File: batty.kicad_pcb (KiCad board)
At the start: 2 copper layers, 137.4 x 95.2 mm, 102 parts, among them J1 MJ-4PP-9, J2 OLED, J3 LED, P1 i2c-pin, P2 i2c-pin, SW1 SW_PUSH, SW10 SW_PUSH, SW11 SW_PUSH, SW12 SW_PUSH, SW13 SW_PUSH, SW14 SW_PUSH, SW15 SW_PUSH, SW16 SW_PUSH, SW17 SW_PUSH, SW18 SW_PUSH, SW19 SW_PUSH, SW2 SW_PUSH, SW20 SW_PUSH, SW21 SW_PUSH, SW22 SW_PUSH, SW23 SW_PUSH, SW3 SW_PUSH, SW4 SW_PUSH, SW5 SW_PUSH, SW6 SW_PUSH, SW7 SW_PUSH, SW8 SW_PUSH, SW9 SW_PUSH, U1 ProMicro

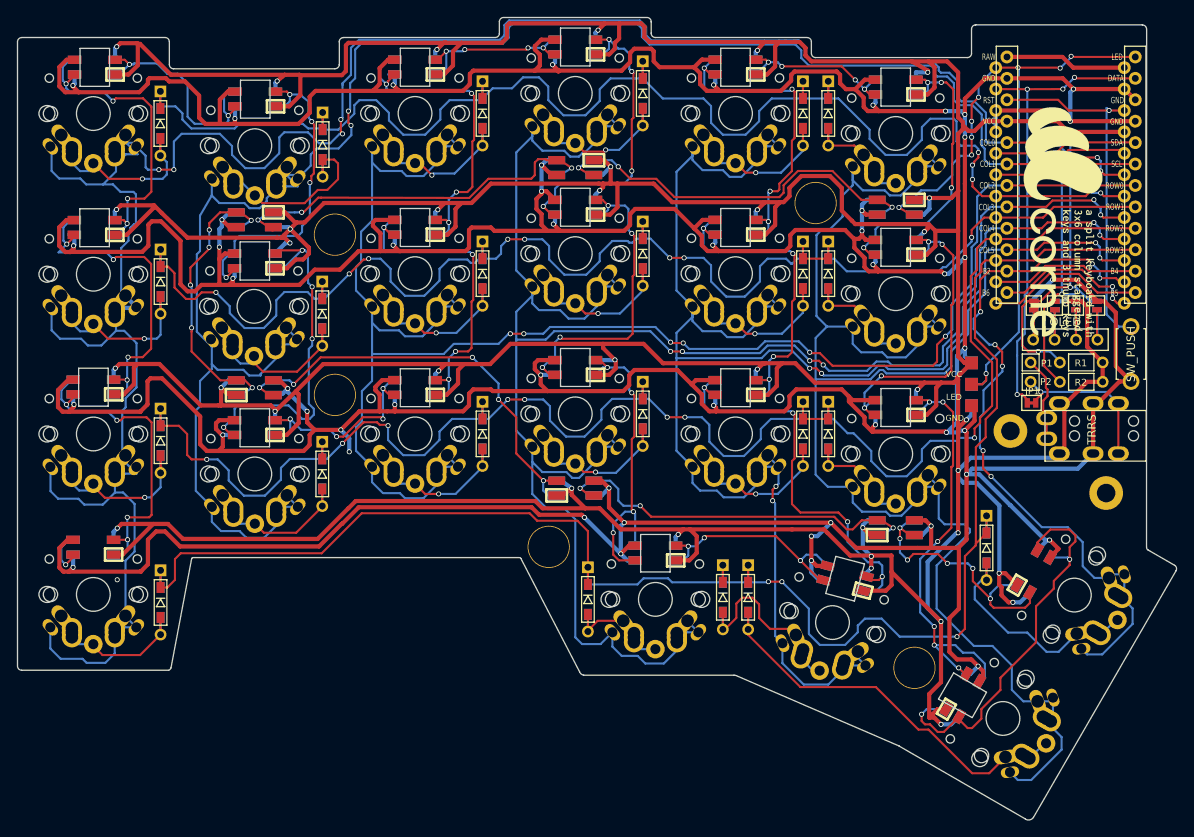
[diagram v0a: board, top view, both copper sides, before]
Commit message: add missing hole, update crkbd logo position.
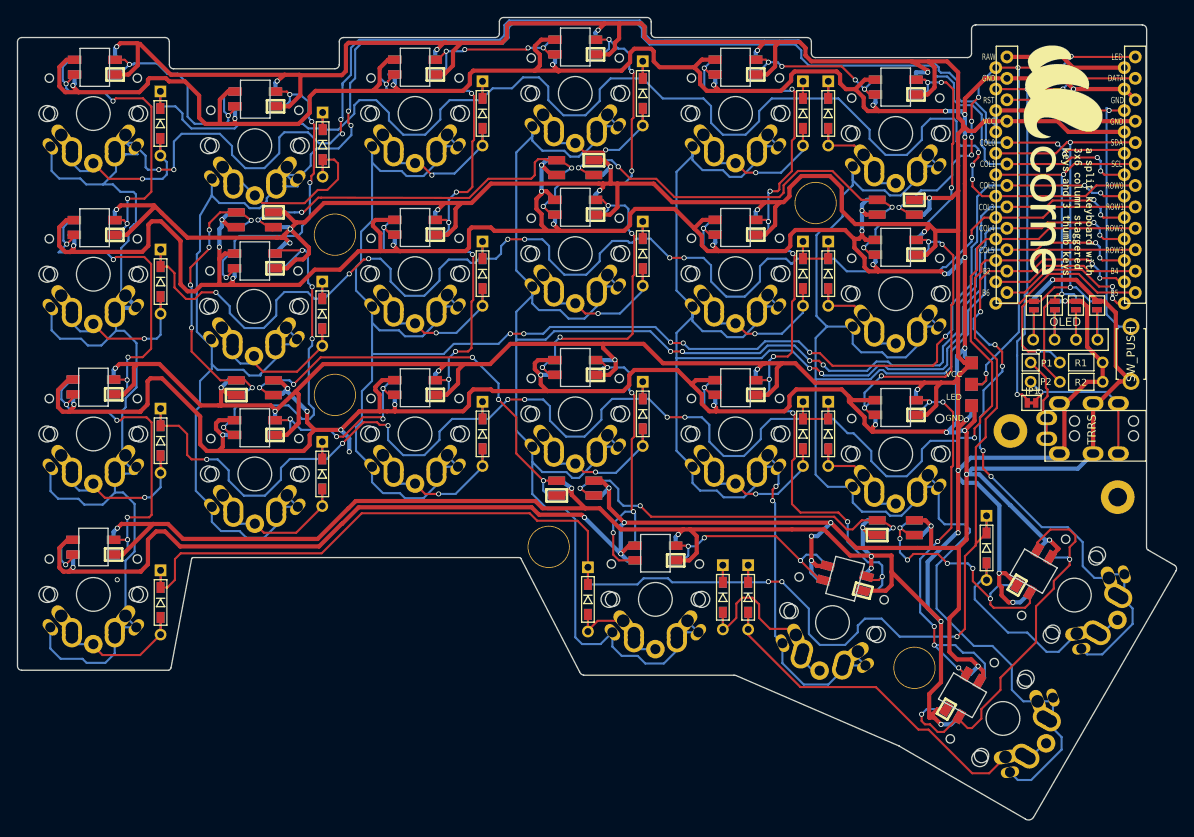
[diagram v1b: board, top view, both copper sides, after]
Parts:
- moved G*** 7.33 mm to (184.7, 78.0)
- moved G*** 7.25 mm to (184.0, 78.0)
- moved ? 1.45 mm to (191.3, 117.9)
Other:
- outline, holes or cut-outs redrawn
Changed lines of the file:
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@@
   (general
     (thickness 1.6)
-    (drawings 148)
+    (drawings 156)
     (tracks 3206)
     (zones 0)
@@
     (34 B.Paste user)
     (35 F.Paste user)
-    (36 B.SilkS user hide)
+    (36 B.SilkS user)
     (37 F.SilkS user)
     (38 B.Mask user)
-    (39 F.Mask user hide)
+    (39 F.Mask user)
     (40 Dwgs.User user)
     (41 Cmts.User user)
@@
     (43 Eco2.User user)
     (44 Edge.Cuts user)
-    (45 Margin user hide)
+    (45 Margin user)
     (46 B.CrtYd user)
     (47 F.CrtYd user)
@@
   )
   (module kbd:corne (layer B.Cu)
-    (at 184 85.25 90)
+    (at 184 78 90)
     (fp_text reference G*** (at 0 0 90) (layer B.SilkS) hide
       (effects (font (size 1.524 1.524) (thickness 0.3)) (justify mirror))
@@
   )
   (module kbd:LEGO_HOLE (layer F.Cu)
-    (at 189.9513 117.392)
+    (at 191.3229 117.8746)
     (descr "Mounting Hole 2.2mm, no annular, M2")
     (tags "mounting hole 2.2mm no annular m2")
@@
   )
   (module kbd:corne (layer F.Cu)
-    (at 184.725 85.325 270)
+    (at 184.725 78 270)
     (fp_text reference G*** (at 0 0 270) (layer F.SilkS) hide
       (effects (font (size 1.524 1.524) (thickness 0.3)))
@@
     (pad "" np_thru_hole circle (at -5.22 4.2 240) (size 1 1) (drill 1) (layers *.Cu *.Mask F.SilkS))
   )
+  (gr_line (start 184.15 126.2634) (end 180.2892 124.0282) (layer Edge.Cuts) (width 0.15))
+  (gr_line (start 182.3974 129.286) (end 184.15 126.2634) (layer Edge.Cuts) (width 0.15))
+  (gr_line (start 178.5366 127.0762) (end 182.3974 129.286) (layer Edge.Cuts) (width 0.15))
+  (gr_line (start 180.2892 124.0282) (end 178.5366 127.0762) (layer Edge.Cuts) (width 0.15))
+  (gr_line (start 71.6026 121.5644) (end 68.1482 121.5644) (layer Edge.Cuts) (width 0.15))
+  (gr_line (start 71.6026 126.0094) (end 71.6026 121.5644) (layer Edge.Cuts) (width 0.15))
+  (gr_line (start 68.1228 126.0094) (end 71.6026 126.0094) (layer Edge.Cuts) (width 0.15))
+  (gr_line (start 68.1228 121.5644) (end 68.1228 126.0094) (layer Edge.Cuts) (width 0.15))
   (dimension 95.75803 (width 0.3) (layer F.SilkS)
     (gr_text "95.758 mm" (at 205.840941 108.844844 89.95440655) (layer F.SilkS)
@@
     (effects (font (size 0.7 0.7) (thickness 0.125)))
   )
-  (gr_line (start 189.9613 117.392) (end 189.9513 117.392) (angle 90) (layer Eco2.User) (width 2.1))
+  (gr_line (start 191.3329 117.8746) (end 191.3229 117.8746) (angle 90) (layer Eco2.User) (width 2.1))
   (gr_line (start 124.2332 122.6738) (end 124.2232 122.6738) (angle 90) (layer Eco2.User) (width 2.5))
   (gr_line (start 155.51 83) (end 155.5 83) (angle 90) (layer Eco2.User) (width 2.5))
